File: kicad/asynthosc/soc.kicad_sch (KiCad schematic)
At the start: 40 parts, among them J11 Conn_01x04_Pin, J6 Conn_01x04_Pin, J9 Conn_01x07_Pin, SW2 SW_Push, U2 STM32H723ZGTx, Y1 8MHz, 8pF

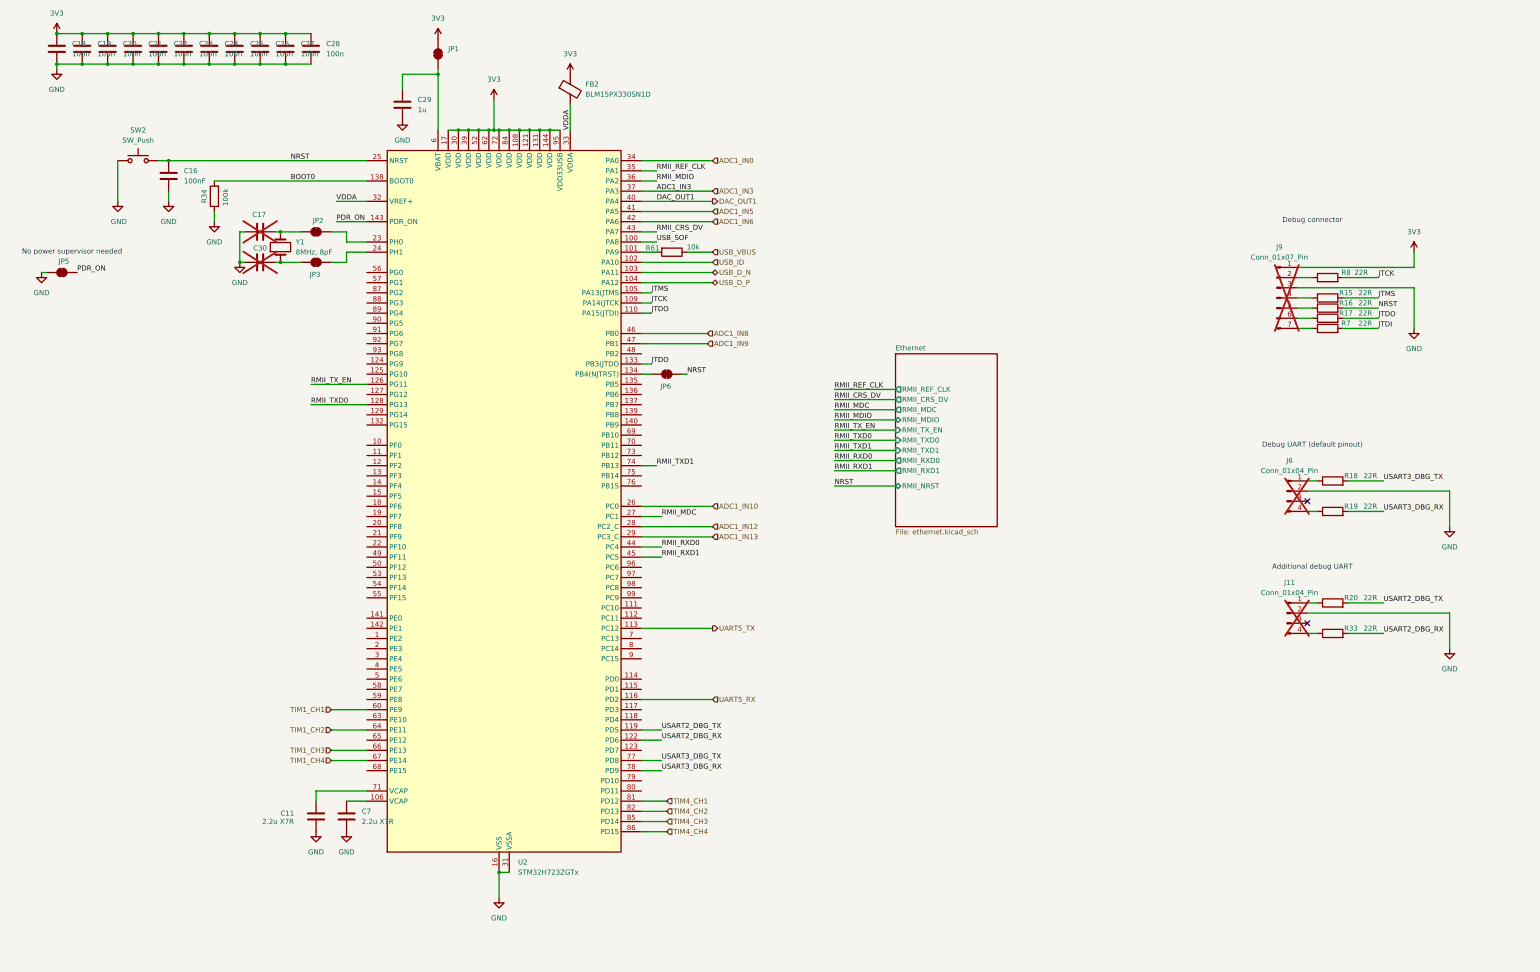
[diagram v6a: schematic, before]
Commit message: sch: add spi nor, display connection, and more footprints
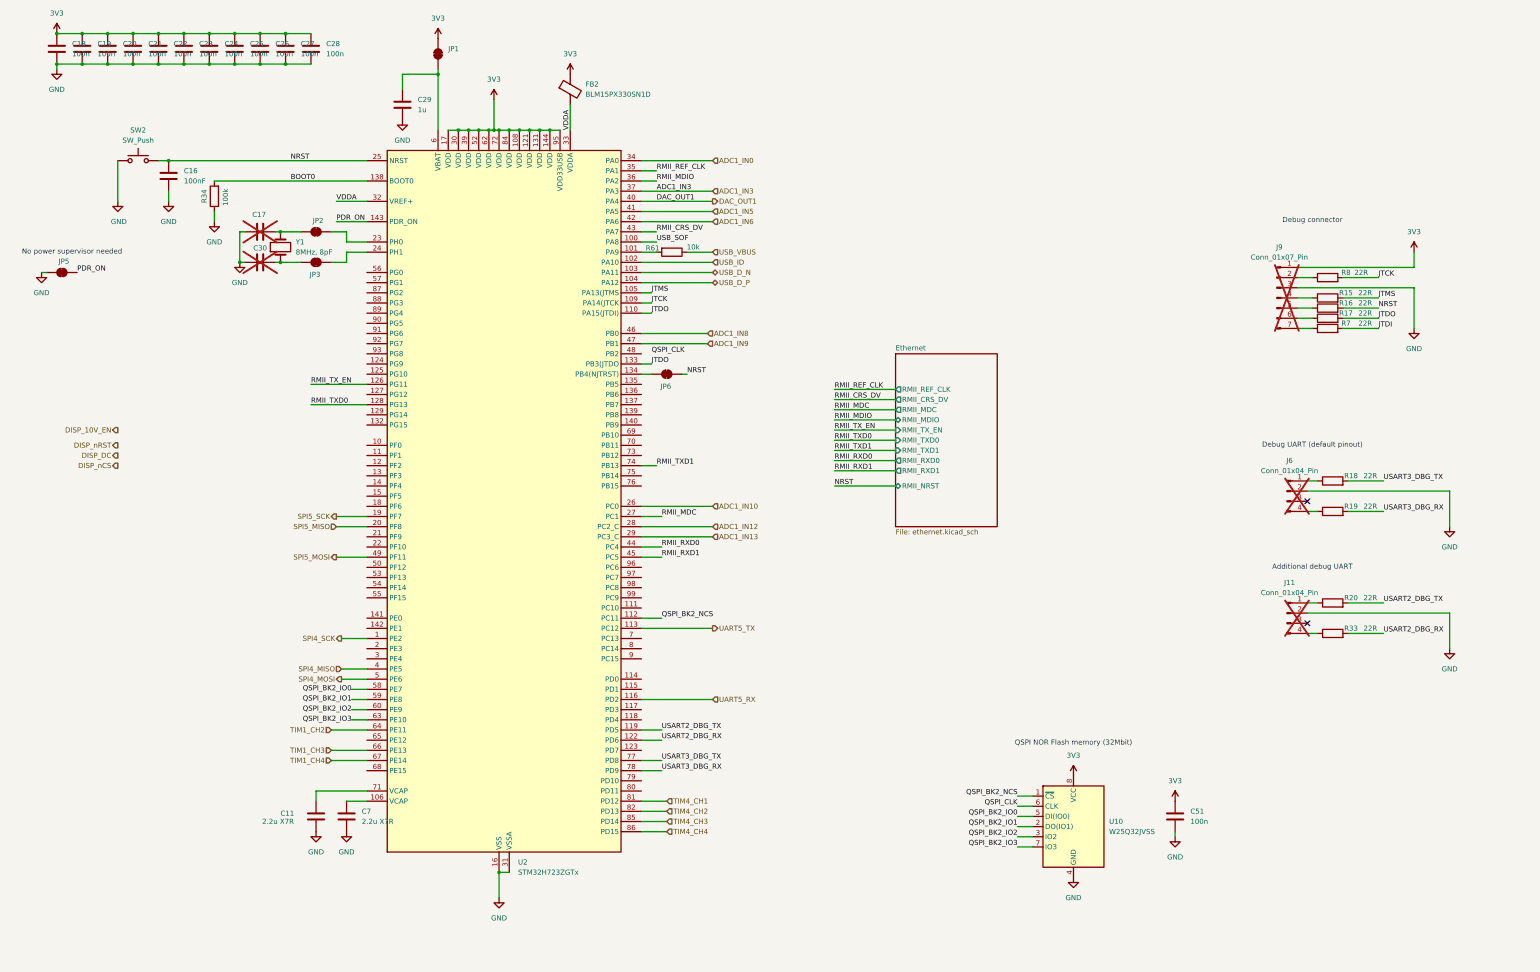
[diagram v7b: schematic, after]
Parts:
- added C51: 100n, symbol Device:C
- added U10: W25Q32JVSS, Package_SO:SOIC-8_5.23x5.23mm_P1.27mm, symbol Memory_Flash:W25Q32JVSS
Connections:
- net 3V3: now also C51.1, U10.8 (VCC)
- net GND: now also C51.2, U10.4 (GND)
- net SPI4_SCK: now reaches U2.1 (PE2)
- net QSPI_BK2_NCS: now reaches U2.112 (PC11)
- net QSPI_BK2_NCS: now also U10.1 (~{CS})
- net SPI5_SCK: now reaches U2.19 (PF7)
- net SPI5_MISO: now reaches U2.20 (PF8)
- net SPI4_MISO: now reaches U2.4 (PE5)
- net SPI5_MOSI: now reaches U2.49 (PF11)
- net SPI4_MOSI: now reaches U2.5 (PE6)
- net QSPI_BK2_IO0: now reaches U2.58 (PE7)
- net QSPI_BK2_IO0: now also U10.5 (DI(IO0))
- net QSPI_BK2_IO1: now reaches U2.59 (PE8)
- net QSPI_BK2_IO1: now also U10.2 (DO(IO1))
- net QSPI_BK2_IO3: now reaches U2.63 (PE10)
- net QSPI_BK2_IO3: now also U10.7 (IO3)
- net TIM1_CH1 renamed QSPI_BK2_IO2
- net QSPI_BK2_IO2: now also U10.3 (IO2)
- new net QSPI_CLK: U10.6 (CLK)
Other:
- note added: "QSPI NOR Flash memory (32Mbit)"

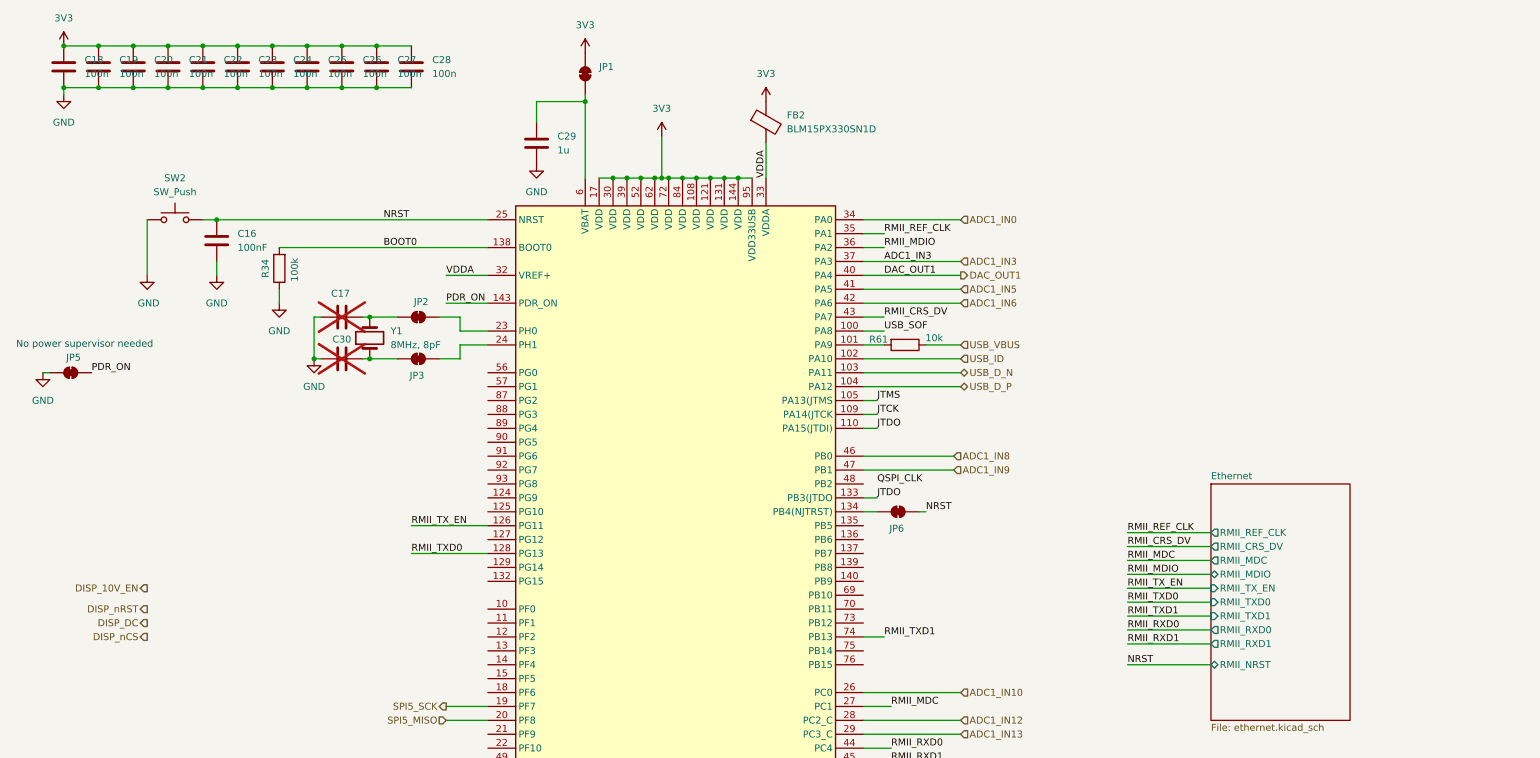
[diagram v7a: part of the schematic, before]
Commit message: sch: power supply improvements
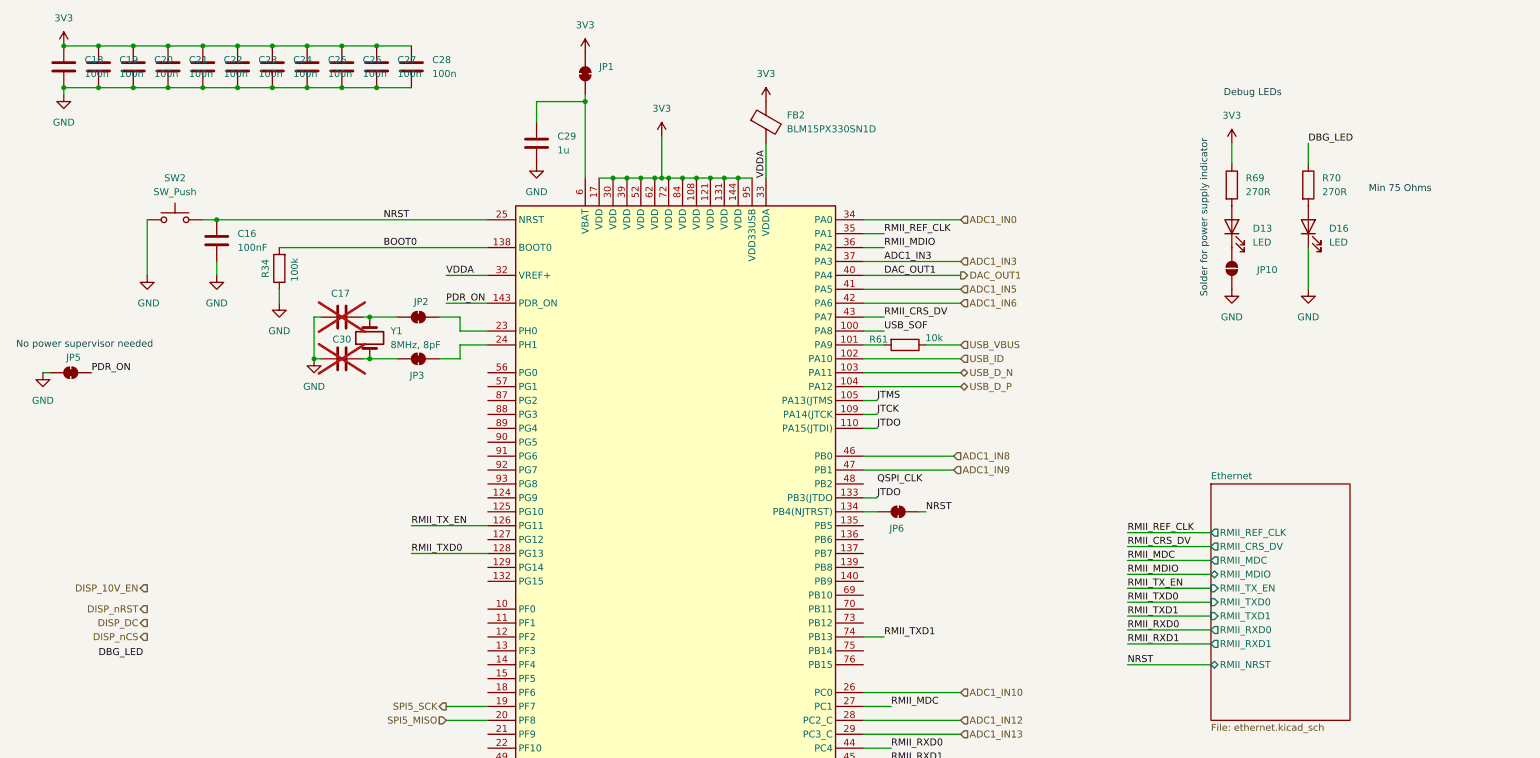
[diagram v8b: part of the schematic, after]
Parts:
- added D13, D16: LED, 0402, symbol Device:LED
- added JP10: SolderJumper_2_Open, symbol Jumper:SolderJumper_2_Open
- added R69, R70: 270R, 0402, symbol Device:R
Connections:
- net 3V3: now also R69.1
- net GND: now also D16.1 (K), JP10.1 (A)
- new net: D16.2 (A), R70.2
- new net: D13.1 (K), JP10.2 (B)
- new net: D13.2 (A), R69.2
- new net DBG_LED: R70.1
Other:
- note added: "Debug LEDs"
- note added: "Min 75 Ohms"
- note added: "Solder for power supply indicator"
